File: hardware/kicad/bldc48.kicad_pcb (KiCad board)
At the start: 4 copper layers, 180 x 69.5 mm, 170 parts, among them J1 BAT+, J10 BRAKE, J11 POWER_BTN, J12 UART, J2 BAT-, J3 MOTOR_A, J4 MOTOR_B, J5 MOTOR_C, J6 SWD, J7 HALL, J8 THROTTLE, J9 FWD/REV, Q1 MMBTA92, Q2 MMBTA42, Q3 IPT015N10N5, Q4 IPT015N10N5, Q5 IPT015N10N5, Q6 IPT015N10N5, Q7 IPT015N10N5, Q8 IPT015N10N5, U1 LM5164DDA, U10 STM32G431CBT6, U2 LM5164DDA, U3 AP2112K-3.3, U4 LM5109BMA, U5 INA240A1D, U6 LM5109BMA, U7 INA240A1D, U8 LM5109BMA, U9 INA240A1D

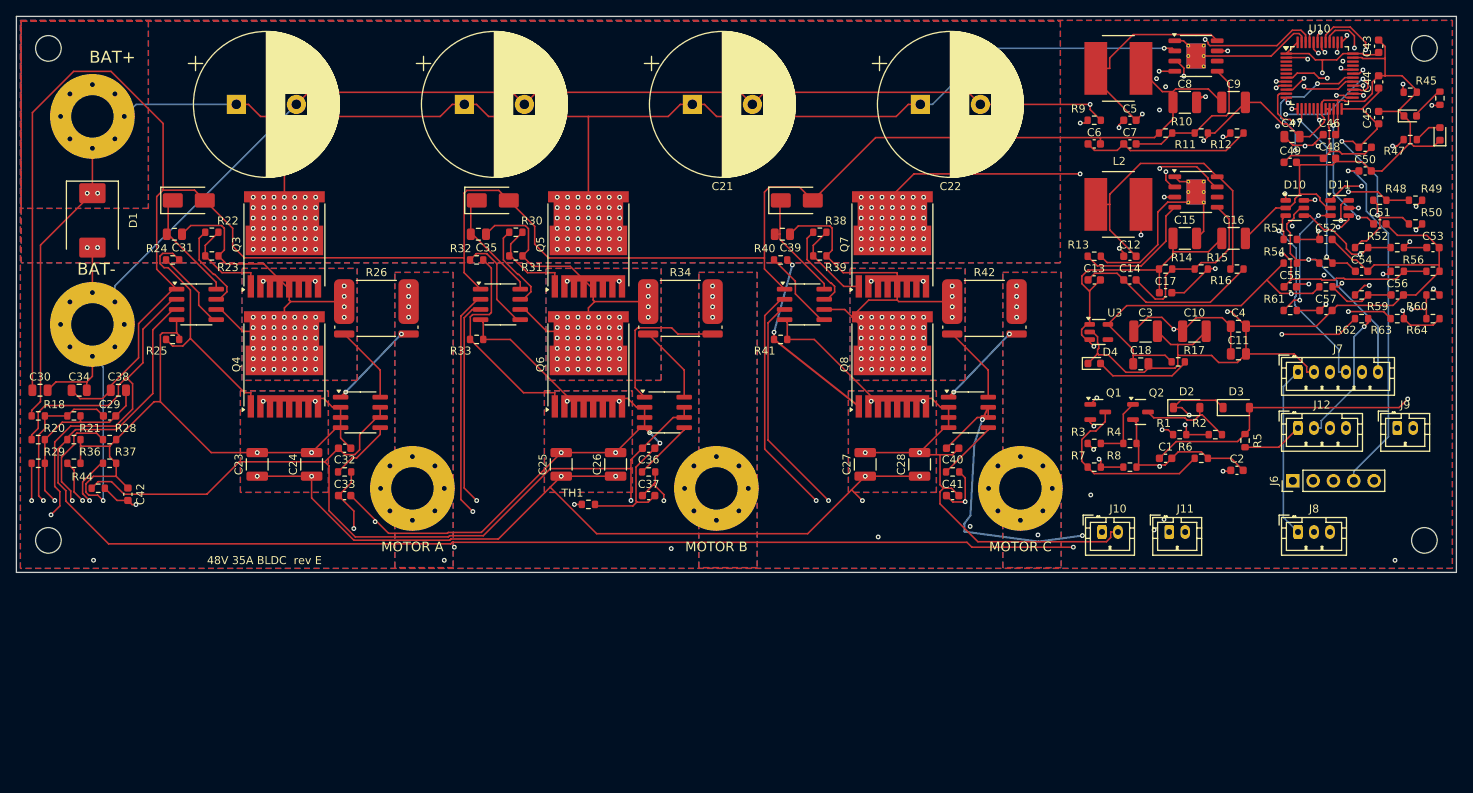
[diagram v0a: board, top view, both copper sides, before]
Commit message: Rev F board: 90 x 95 mm, 4 layers, two-sided, fully routed, DRC 0 violations / 0 unconnected
Default board height 95 mm; SES placement restore fixed for back-side parts at 90/270 deg;
silkscreen title and BAT- label moved clear of pads.

Co-Authored-By: Claude Opus 5.5 <noreply@anthropic.com>
Claude-Session: https://claude.ai/code/session_01KE5bAkgcicsoh5erUtagKE
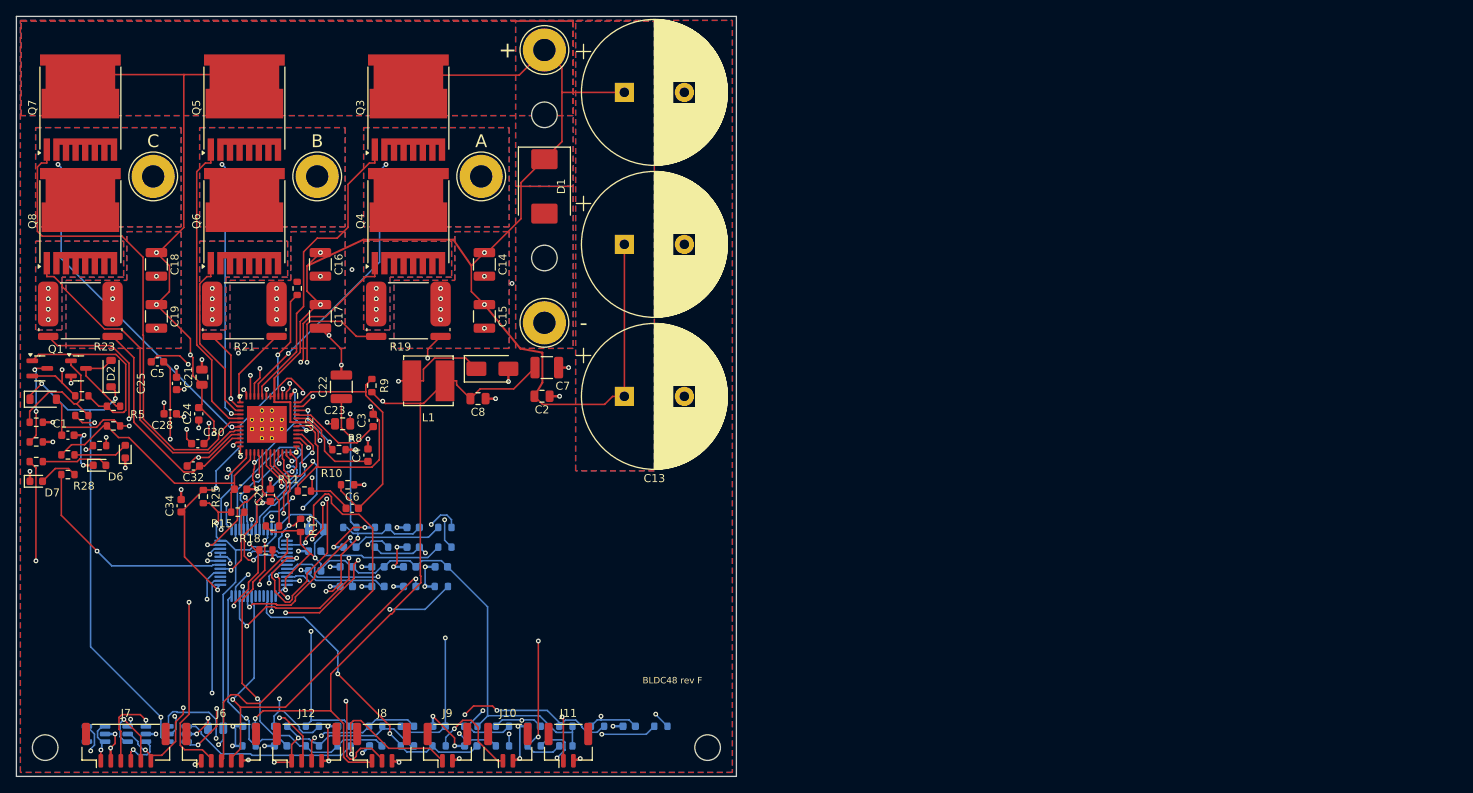
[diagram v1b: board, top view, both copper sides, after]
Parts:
- removed C50, C54, C55, C56, C57: 100n, Capacitor_SMD:C_0603_1608Metric
- removed C51, C52, C53: 1n, Capacitor_SMD:C_0603_1608Metric
- removed D10, D11: ESDA6V1-5SC6, Package_TO_SOT_SMD:SOT-23-6
- removed L2: 33u, Inductor_SMD:L_Bourns_SRN8040TA
- removed R46, R47, R49, R51, R53, R55, R59, R61: 1k, Resistor_SMD:R_0603_1608Metric
- removed R48, R50, R52: 2.2k, Resistor_SMD:R_0603_1608Metric
- removed R54, R58, R60, R64: 10k, Resistor_SMD:R_0603_1608Metric
- removed R56: 12k, Resistor_SMD:R_0603_1608Metric
- removed R57: 22k, Resistor_SMD:R_0603_1608Metric
- removed R62, R63: 100R, Resistor_SMD:R_0603_1608Metric
- removed U10: STM32G431CBT6, Package_QFP:LQFP-48_7x7mm_P0.5mm
- removed U4, U6, U8: LM5109BMA, Package_SO:SOIC-8_3.9x4.9mm_P1.27mm
- removed U5, U7, U9: INA240A1D, Package_SO:SOIC-8_3.9x4.9mm_P1.27mm
- C10: value 2.2u/100V -> 4.7u; footprint Capacitor_SMD:C_1210_3225Metric -> Capacitor_SMD:C_0805_2012Metric; moved to B.Cu
- C11: value 100n/100V -> 1000u/100V; footprint Capacitor_SMD:C_0805_2012Metric -> Capacitor_THT:CP_Radial_D18.0mm_P7.50mm
- C12: value 2.2n -> 1000u/100V; footprint Capacitor_SMD:C_0603_1608Metric -> Capacitor_THT:CP_Radial_D18.0mm_P7.50mm
- C13: value 3.3n -> 1000u/100V; footprint Capacitor_SMD:C_0603_1608Metric -> Capacitor_THT:CP_Radial_D18.0mm_P7.50mm
- C14: value 100n -> 2.2u/100V; footprint Capacitor_SMD:C_0603_1608Metric -> Capacitor_SMD:C_1210_3225Metric
- C15, C16: value 22u/10V -> 2.2u/100V
- C17: value 1u -> 2.2u/100V; footprint Capacitor_SMD:C_0603_1608Metric -> Capacitor_SMD:C_1210_3225Metric
- C18: value 4.7u -> 2.2u/100V; footprint Capacitor_SMD:C_0805_2012Metric -> Capacitor_SMD:C_1210_3225Metric
- C19, C22: value 1000u/100V -> 2.2u/100V; footprint Capacitor_THT:CP_Radial_D18.0mm_P7.50mm -> Capacitor_SMD:C_1210_3225Metric
- C2: value 1n -> 1u/100V; footprint Capacitor_SMD:C_0603_1608Metric -> Capacitor_SMD:C_0805_2012Metric
- C20: value 1000u/100V -> 10n; footprint Capacitor_THT:CP_Radial_D18.0mm_P7.50mm -> Capacitor_SMD:C_0603_1608Metric; moved to B.Cu
- C21: value 1000u/100V -> 100n/100V; footprint Capacitor_THT:CP_Radial_D18.0mm_P7.50mm -> Capacitor_SMD:C_0805_2012Metric
- C23: value 2.2u/100V -> 47n/100V; footprint Capacitor_SMD:C_1210_3225Metric -> Capacitor_SMD:C_0805_2012Metric
- C24, C25: value 2.2u/100V -> 1u/16V; footprint Capacitor_SMD:C_1210_3225Metric -> Capacitor_SMD:C_0603_1608Metric
- C26: value 2.2u/100V -> 1u; footprint Capacitor_SMD:C_1210_3225Metric -> Capacitor_SMD:C_0603_1608Metric
- C27: value 2.2u/100V -> 100n; footprint Capacitor_SMD:C_1210_3225Metric -> Capacitor_SMD:C_0603_1608Metric
- C28: value 2.2u/100V -> 1n; footprint Capacitor_SMD:C_1210_3225Metric -> Capacitor_SMD:C_0603_1608Metric
- C29: value 10n -> 1n; moved to B.Cu
- C3: value 2.2u/100V -> 10n; footprint Capacitor_SMD:C_1210_3225Metric -> Capacitor_SMD:C_0603_1608Metric
- C30: value 1u/25V -> 1n; footprint Capacitor_SMD:C_0805_2012Metric -> Capacitor_SMD:C_0603_1608Metric
- C31: value 2.2u/25V -> 1n; footprint Capacitor_SMD:C_0805_2012Metric -> Capacitor_SMD:C_0603_1608Metric; moved to B.Cu
- C32: value 100n -> 1n
- C33, C36, C42, C46, C49, FB1, R39, R41, R43, R45: moved to B.Cu
- C34: value 1u/25V -> 100n; footprint Capacitor_SMD:C_0805_2012Metric -> Capacitor_SMD:C_0603_1608Metric
- C35: value 2.2u/25V -> 100n; footprint Capacitor_SMD:C_0805_2012Metric -> Capacitor_SMD:C_0603_1608Metric; moved to B.Cu
- C37, C41: value 1n -> 100n; moved to B.Cu
- C38: value 1u/25V -> 100n; footprint Capacitor_SMD:C_0805_2012Metric -> Capacitor_SMD:C_0603_1608Metric; moved to B.Cu
- C39: value 2.2u/25V -> 4.7u; moved to B.Cu
- C4: value 100n/100V -> 1u; footprint Capacitor_SMD:C_0805_2012Metric -> Capacitor_SMD:C_0603_1608Metric
- C40: value 100n -> 1u; moved to B.Cu
- C43, C44, C45: value 100n -> 1n; moved to B.Cu
- C47: value 4.7u -> 100n; footprint Capacitor_SMD:C_0805_2012Metric -> Capacitor_SMD:C_0603_1608Metric; moved to B.Cu
- C48: value 1u -> 100n; moved to B.Cu
- C5: value 2.2n -> 47n
- C6: value 3.3n -> 330p
- C7: value 100n -> 22u/10V; footprint Capacitor_SMD:C_0603_1608Metric -> Capacitor_SMD:C_1210_3225Metric
- C8: value 22u/25V -> 4.7u; footprint Capacitor_SMD:C_1210_3225Metric -> Capacitor_SMD:C_0805_2012Metric
- C9: value 22u/25V -> 1u; footprint Capacitor_SMD:C_1210_3225Metric -> Capacitor_SMD:C_0603_1608Metric; moved to B.Cu
- D4: value GREEN -> SS110; footprint LED_SMD:LED_0603_1608Metric -> Diode_SMD:D_SMA
- D5, D6: value ES1D -> GREEN; footprint Diode_SMD:D_SMA -> LED_SMD:LED_0603_1608Metric
- D7: value ES1D -> RED; footprint Diode_SMD:D_SMA -> LED_SMD:LED_0603_1608Metric
- D8: value GREEN -> ESDA6V1-5SC6; footprint LED_SMD:LED_0603_1608Metric -> Package_TO_SOT_SMD:SOT-23-6; moved to B.Cu
- D9: value RED -> ESDA6V1-5SC6; footprint LED_SMD:LED_0603_1608Metric -> Package_TO_SOT_SMD:SOT-23-6; moved to B.Cu
- J1, J2, J3, J4, J5: footprint MountingHole:MountingHole_5.3mm_M5_Pad_Via -> bldc48:SolderWire_12AWG_D2.8mm_OD5.4mm
- J10, J11, J9: footprint Connector_JST:JST_PH_B2B-PH-K_1x02_P2.00mm_Vertical -> Connector_JST:JST_GH_BM02B-GHS-TBT_1x02-1MP_P1.25mm_Vertical
- J12: footprint Connector_JST:JST_PH_B4B-PH-K_1x04_P2.00mm_Vertical -> Connector_JST:JST_GH_BM04B-GHS-TBT_1x04-1MP_P1.25mm_Vertical
- J6: footprint Connector_PinHeader_2.54mm:PinHeader_1x05_P2.54mm_Vertical -> Connector_JST:JST_GH_BM05B-GHS-TBT_1x05-1MP_P1.25mm_Vertical
- J7: footprint Connector_JST:JST_PH_B6B-PH-K_1x06_P2.00mm_Vertical -> Connector_JST:JST_GH_BM06B-GHS-TBT_1x06-1MP_P1.25mm_Vertical
- J8: footprint Connector_JST:JST_PH_B3B-PH-K_1x03_P2.00mm_Vertical -> Connector_JST:JST_GH_BM03B-GHS-TBT_1x03-1MP_P1.25mm_Vertical
- L1: value 68u -> 100u; footprint Inductor_SMD:L_Bourns_SRN8040TA -> Inductor_SMD:L_Bourns_SRN6045TA
- R10: value 90.9k -> 4.02k
- R11: value 10k -> 8.2k
- R12: value 365k -> 2.2k
- R13: value 41.2k -> 100k; moved to B.Cu
- R14: value 31.6k -> 5.6k; moved to B.Cu
- R16: value 178k -> 4.7k
- R17: value 2.2k -> 10k
- R19: value 5.6k -> 0.5m; footprint Resistor_SMD:R_0603_1608Metric -> Resistor_SMD:R_Shunt_Isabellenhuette_BVR4026
- R20, R44: value 10k -> 100R; moved to B.Cu
- R21, R23: value 10k -> 0.5m; footprint Resistor_SMD:R_0603_1608Metric -> Resistor_SMD:R_Shunt_Isabellenhuette_BVR4026
- R22, R24: value 4R7 -> 100R; moved to B.Cu
- R26: value 0.5m -> 10k; footprint Resistor_SMD:R_Shunt_Isabellenhuette_BVR4026 -> Resistor_SMD:R_0603_1608Metric; moved to B.Cu
- R27: value 100R -> 1k
- R28: value 10k -> 1k
- R29, R31, R33: value 10k -> 2.2k; moved to B.Cu
- R30, R32, R40: value 4R7 -> 1k; moved to B.Cu
- R34, R42: value 0.5m -> 1k; footprint Resistor_SMD:R_Shunt_Isabellenhuette_BVR4026 -> Resistor_SMD:R_0603_1608Metric; moved to B.Cu
- R35: value 100R -> 10k; moved to B.Cu
- R36: value 10k -> 1k; moved to B.Cu
- R37: value 10k -> 12k; moved to B.Cu
- R38: value 4R7 -> 22k; moved to B.Cu
- R7: value 330k -> 150k
- R8: value 27k -> 100k
- R9: value 100k -> 4.02k
- U1: value LM5164DDA -> AP2112K-3.3; footprint Package_SO:HSOP-8-1EP_3.9x4.9mm_P1.27mm_EP2.41x3.1mm_ThermalVias -> Package_TO_SOT_SMD:SOT-23-5; moved to B.Cu
- U2: value LM5164DDA -> DRV8353RS; footprint Package_SO:HSOP-8-1EP_3.9x4.9mm_P1.27mm_EP2.41x3.1mm_ThermalVias -> bldc48:TI-RGZ-48-QFN
- U3: value AP2112K-3.3 -> STM32G431CBT6; footprint Package_TO_SOT_SMD:SOT-23-5 -> Package_QFP:LQFP-48_7x7mm_P0.5mm; moved to B.Cu
- moved D8 176.9 mm to (15.0, 89.7), turned to 180 degrees
- moved D9 174.7 mm to (20.1, 89.7), turned to 180 degrees
- moved U1 161.5 mm to (9.95, 89.7), turned to 180 degrees
- moved C43 154.8 mm to (41.0, 88.7), turned to 180 degrees
- moved J7 153.8 mm to (13.7, 91.1)
- moved R12 151.6 mm to (6.44, 54.8)
- moved D3 149.1 mm to (3.35, 47.8)
- moved C47 147.6 mm to (33.0, 91.2), turned to 180 degrees
- moved C9 145.7 mm to (29.1, 88.7), turned to 180 degrees
- moved R6 145.6 mm to (2.48, 53.2)
- moved C44 142.4 mm to (52.8, 88.7), turned to 180 degrees
- moved FB1 141.6 mm to (37.3, 69.3), turned to 180 degrees
- moved R5 141.5 mm to (12.1, 51.2), turned to 0 degrees
- moved C48 140.0 mm to (44.9, 91.2), turned to 180 degrees
- moved J6 138.0 mm to (25.6, 91.1), turned to 0 degrees
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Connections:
- C10 pad 1: +48V -> +3V3
- C12 pad 1: BST5 -> +48V
- C12 pad 2: SW5 -> GND
- C13 pad 1: RIP5 -> +48V
- C13 pad 2: +5V -> GND
- C14 pad 1: RIP5 -> +48V
- C14 pad 2: FB5 -> GND
- C15 pad 1: +5V -> +48V
- C16 pad 1: +5V -> +48V
- C17 pad 1: +5V -> +48V
- C18 pad 1: +3V3 -> +48V
- C2 pad 1: BUCK_EN -> +48V
- C20 pad 1: +48V -> VBUS_SENSE
- C23 pad 1: +48V -> CPL
- C23 pad 2: GND -> CPH
- C24 pad 1: +48V -> VCP
- C24 pad 2: GND -> +48V
- C25 pad 1: +48V -> VGLS
- C26 pad 1: +48V -> DVDD
- C27 pad 1: +48V -> +3V3
- C28 pad 1: +48V -> SP_A
- C28 pad 2: GND -> SN_A
- C29 pad 1: VBUS_SENSE -> ISENSE_A
- C3 pad 1: +48V -> BST5
- C3 pad 2: GND -> SW5
- C30 pad 1: +12V -> SP_B
- C30 pad 2: GND -> SN_B
- C31 pad 1: HB_A -> ISENSE_B
- C31 pad 2: SW_A -> GND
- C32 pad 1: +3V3 -> SP_C
- C32 pad 2: GND -> SN_C
- C33 pad 1: ISENSE_A -> ISENSE_C
- C34 pad 1: +12V -> TEMP_FET
- C35 pad 1: HB_B -> +3V3
- C35 pad 2: SW_B -> GND
- C37 pad 1: ISENSE_B -> +3V3
- C38 pad 1: +12V -> +3V3
- C39 pad 1: HB_C -> +3V3
- C39 pad 2: SW_C -> GND
- C4 pad 1: +48V -> VCC_B
- C40 pad 1: +3V3 -> +3V3A
- C41 pad 1: ISENSE_C -> +3V3A
- C42 pad 1: TEMP_FET -> NRST
- C43 pad 1: +3V3 -> HALL_A
- C44 pad 1: +3V3 -> HALL_B
- C45 pad 1: +3V3 -> HALL_C
- C46 pad 1: +3V3 -> TEMP_MOTOR
- C47 pad 1: +3V3 -> THROTTLE
- C48 pad 1: +3V3A -> DIR_SW
- C49 pad 1: +3V3A -> BRAKE
- C5 pad 1: BST12 -> RIP5
- C5 pad 2: SW12 -> +5V
- C6 pad 1: RIP12 -> RIP5
- C6 pad 2: +12V -> FB5
- C7 pad 1: RIP12 -> +5V
- C7 pad 2: FB12 -> GND
- C8 pad 1: +12V -> +5V
- C9 pad 1: +12V -> +5V
- D4 pad 1: GND -> SW5
- D4 pad 2: PWR_LED_A -> GND
- D5 pad 1: HB_A -> GND
- D5 pad 2: +12V -> PWR_LED_A
- D6 pad 1: HB_B -> GND
- D6 pad 2: +12V -> LED_STATUS_A
- D7 pad 1: HB_C -> GND
- D7 pad 2: +12V -> LED_FAULT_A
- D8 pad 1: GND -> HALL_A_IN
- D8 pad 2: LED_STATUS_A -> GND
- D9 pad 1: GND -> DIR_IN
- D9 pad 2: LED_FAULT_A -> GND
- J3 pad 1: PHASE_A -> SW_A
- J4 pad 1: PHASE_B -> SW_B
- J5 pad 1: PHASE_C -> SW_C
- L1 pad 1: SW12 -> SW5
- L1 pad 2: +12V -> +5V
- Q4 pad 2: GND -> LS_A
- Q6 pad 2: GND -> LS_B
- Q8 pad 2: GND -> LS_C
- R10 pad 1: +12V -> FB5
- R10 pad 2: FB12 -> GND
- R11 pad 1: FB12 -> SW5
- R11 pad 2: GND -> RIP5
- R12 pad 1: SW12 -> +3V3
- R12 pad 2: RIP12 -> PWR_LED_A
- R13 pad 1: RON5 -> +48V
- R13 pad 2: GND -> VBUS_SENSE
- R14 pad 1: +5V -> VBUS_SENSE
- R14 pad 2: FB5 -> GND
- R15 pad 1: FB5 -> +3V3
- R15 pad 2: GND -> DRV_FAULT
- R16 pad 1: SW5 -> +3V3
- R16 pad 2: RIP5 -> DRV_SDO
- R17 pad 2: PWR_LED_A -> DRV_CS
- R18 pad 1: +48V -> DRV_EN
- R18 pad 2: VBUS_SENSE -> GND
- R19 pad 1: VBUS_SENSE -> LS_A
- R19 pad 2: GND -> SP_A
- R20 pad 1: PWM_AH -> SO_A
- R20 pad 2: GND -> ISENSE_A
- R21 pad 1: PWM_AL -> LS_B
- R21 pad 2: GND -> SP_B
- R22 pad 1: HO_A -> SO_B
- R22 pad 2: GH_A -> ISENSE_B
- R23 pad 1: GH_A -> LS_C
- R23 pad 2: SW_A -> SP_C
- R24 pad 1: LO_A -> SO_C
- R24 pad 2: GL_A -> ISENSE_C
- R25 pad 1: GL_A -> +3V3
- R25 pad 2: GND -> TEMP_FET
- R26 pad 1: SW_A -> BOOT0
- R26 pad 2: ISP_A -> GND
- R27 pad 1: ISO_A -> LED_STATUS
- R27 pad 2: ISENSE_A -> LED_STATUS_A
- R28 pad 1: PWM_BH -> LED_FAULT
- R28 pad 2: GND -> LED_FAULT_A
- R29 pad 1: PWM_BL -> +3V3
- R29 pad 2: GND -> HALL_A_IN
- R30 pad 1: HO_B -> HALL_A_IN
- R30 pad 2: GH_B -> HALL_A
- R31 pad 1: GH_B -> +3V3
- R31 pad 2: SW_B -> HALL_B_IN
- R32 pad 1: LO_B -> HALL_B_IN
- R32 pad 2: GL_B -> HALL_B
- R33 pad 1: GL_B -> +3V3
- R33 pad 2: GND -> HALL_C_IN
- R34 pad 1: SW_B -> HALL_C_IN
- R34 pad 2: ISP_B -> HALL_C
- R35 pad 1: ISO_B -> +3V3
- R35 pad 2: ISENSE_B -> MTEMP_IN
- R36 pad 1: PWM_CH -> MTEMP_IN
- R36 pad 2: GND -> TEMP_MOTOR
- R37 pad 1: PWM_CL -> THR_IN
- R37 pad 2: GND -> THROTTLE
- R38 pad 1: HO_C -> THROTTLE
- R38 pad 2: GH_C -> GND
- R39 pad 1: GH_C -> +3V3
- R39 pad 2: SW_C -> DIR_SW
- R40 pad 1: LO_C -> DIR_IN
- R40 pad 2: GL_C -> DIR_SW
- R41 pad 1: GL_C -> +3V3
- R41 pad 2: GND -> BRAKE
- R42 pad 1: SW_C -> BRAKE_IN
- R42 pad 2: ISP_C -> BRAKE
- R43 pad 1: ISO_C -> UART_TX
- R43 pad 2: ISENSE_C -> UART_TX_C
- R44 pad 1: +3V3 -> UART_RX_C
- R44 pad 2: TEMP_FET -> UART_RX
- R45 pad 1: BOOT0 -> +3V3
- R45 pad 2: GND -> UART_RX
- R7 pad 2: BUCK_EN -> RT_SD
- R8 pad 1: BUCK_EN -> RCL
- R9 pad 1: RON12 -> +5V
- R9 pad 2: GND -> FB5
- U1 pad 1: GND -> +5V
- U1 pad 2: +48V -> GND
- U1 pad 3: BUCK_EN -> +5V
- U1 pad 4: RON12 -> (no net)
- U1 pad 5: FB12 -> +3V3
- U2 pad 2: +48V -> VGLS
- U2 pad 3: BUCK_EN -> CPL
- U2 pad 4: RON5 -> CPH
- U2 pad 5: FB5 -> +48V
- U2 pad 6: (no net) -> +48V
- U2 pad 7: BST5 -> VCP
- U2 pad 8: SW5 -> GH_A
- U2 pad 9: GND -> SW_A
- U3 pad 1: +5V -> +3V3
- U3 pad 2: GND -> LED_STATUS
- U3 pad 3: +5V -> BRAKE
- U3 pad 5: +3V3 -> (no net)
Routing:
- net GND: track 948.5 -> 304.7 mm, vias 26 -> 82
- net +12V: track 283.7 -> 0.00 mm
- net PWM_BL: track 278.4 -> 14.7 mm, vias 6 -> 1
- net PWM_AH: track 269.5 -> 22.2 mm, vias 4 -> 3
- net PWM_CH: track 254.3 -> 14.1 mm, vias 6 -> 1
- net PWM_BH: track 252.3 -> 12.4 mm, vias 5 -> 1
- net PWM_AL: track 242.3 -> 18.8 mm, vias 3 -> 1
- net +3V3: track 425.2 -> 217.6 mm, vias 11 -> 8
- net PWM_CL: track 244.9 -> 38.8 mm, vias 5 -> 2
- net +48V: track 499.9 -> 302.4 mm, vias 141 -> 11
- net VBUS_SENSE: track 226.2 -> 34.1 mm
- net TEMP_FET: track 194.5 -> 46.4 mm
- net ISENSE_A: track 166.5 -> 31.2 mm, vias 3 -> 2
- net ISENSE_B: track 127.5 -> 36.8 mm, vias 2 -> 4
- net BUCK_EN: track 79.0 -> 0.00 mm, vias 4 -> 0
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- added copper zone on B.Cu, net LS_A
- added copper zone on F.Cu, net LS_A
- added copper zone on B.Cu, net LS_B
- added copper zone on F.Cu, net LS_B
- added copper zone on B.Cu, net LS_C
- added copper zone on F.Cu, net LS_C
- removed copper zone on B.Cu, net PHASE_A
- removed copper zone on F.Cu, net PHASE_A
- removed copper zone on B.Cu, net PHASE_B
- removed copper zone on F.Cu, net PHASE_B
- removed copper zone on B.Cu, net PHASE_C
- removed copper zone on F.Cu, net PHASE_C
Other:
- board size 180 x 69.5 mm -> 90 x 95 mm
- board text added: "+"
- board text added: "-"
- board text added: "A"
- board text added: "B"
- board text added: "BLDC48 rev F"
- board text added: "C"
- board text removed: "48V 35A BLDC rev E"
- board text removed: "BAT+"
- board text removed: "BAT-"
- board text removed: "MOTOR A"
- board text removed: "MOTOR B"
- board text removed: "MOTOR C"
